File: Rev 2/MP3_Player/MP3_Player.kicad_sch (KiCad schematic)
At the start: 1 part, among them U1 ESP32-WROOM-32

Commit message: added some parts
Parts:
- added J1: AudioJack3_SwitchT, symbol Connector_Audio:AudioJack3_SwitchT
- added M1: Haptic Feedback, symbol Motor:Motor_DC
- added SW1: RotaryEncoder_Switch, symbol Device:RotaryEncoder_Switch
- added SW2, SW3, SW4, SW5: SW_SPST, symbol Switch:SW_SPST
- added U2: ~, Subsystem Main:2.4'_TFT_SPI_ILI9341_WITH_SD_CARD, symbol MP3_Player_Custom_Parts:2.4'_TFT_SPI_ILI9341_WITH_SD_CARD

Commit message: Finished Setup
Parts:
- added L_SPKR1, RSPKR1: ~, MP3_Player_Custom_Footprints:MAX98357 I2C Audio Driver, symbol MP3_Player_Custom_Parts:Adafruit_MAX98357
- added Q1: NPN, Package_TO_SOT_THT:TO-92L_Inline, symbol Simulation_SPICE:NPN
- added R1, R2, R3, R4, R5, R6: 10K, Resistor_THT:R_Axial_DIN0204_L3.6mm_D1.6mm_P7.62mm_Horizontal, symbol Device:R
- added R7: R, Resistor_THT:R_Axial_DIN0204_L3.6mm_D1.6mm_P7.62mm_Horizontal, symbol Device:R
- added SW4: Power, Button_Switch_THT:SW_Slide_SPDT_Angled_CK_OS102011MA1Q, symbol Switch:SW_SPDT
- added SW6: Hold, Button_Switch_THT:SW_Slide_SPDT_Angled_CK_OS102011MA1Q, symbol Switch:SW_SPDT
- ESP32: renamed from U1; footprint RF_Module:ESP32-WROOM-32 -> MP3_Player_Custom_Footprints:Wemos Lolin32 Lite v1.0.0
- J1: footprint (none) -> Connector_Audio:Jack_3.5mm_CUI_SJ1-3524N_Horizontal
- M1: footprint (none) -> TerminalBlock_RND:TerminalBlock_RND_205-00001_1x02_P5.00mm_Horizontal
- Primary Rotary Encoder1: renamed from SW1; footprint (none) -> Rotary_Encoder:RotaryEncoder_Alps_EC11E-Switch_Vertical_H20mm
- SW1: renamed from SW2; value SW_SPST -> Home; footprint (none) -> keyswitches:Kailh_socket_PG1350
- SW2: renamed from SW4; value SW_SPST -> Back; footprint (none) -> keyswitches:Kailh_socket_PG1350
- SW3: value SW_SPST -> Play/Pause; footprint (none) -> keyswitches:Kailh_socket_PG1350
- SW5: value SW_SPST -> Menu; footprint (none) -> keyswitches:Kailh_socket_PG1350
- Screen&SDCardReader1: renamed from U2; footprint Subsystem Main:2.4'_TFT_SPI_ILI9341_WITH_SD_CARD -> MP3_Player_Custom_Footprints:2.4'_TFT_SPI_ILI9341_WITH_SD_CARD
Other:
- moved on the sheet: ESP32, J1, M1, Primary Rotary Encoder1, SW1, SW2, SW3, SW5, Screen&SDCardReader1

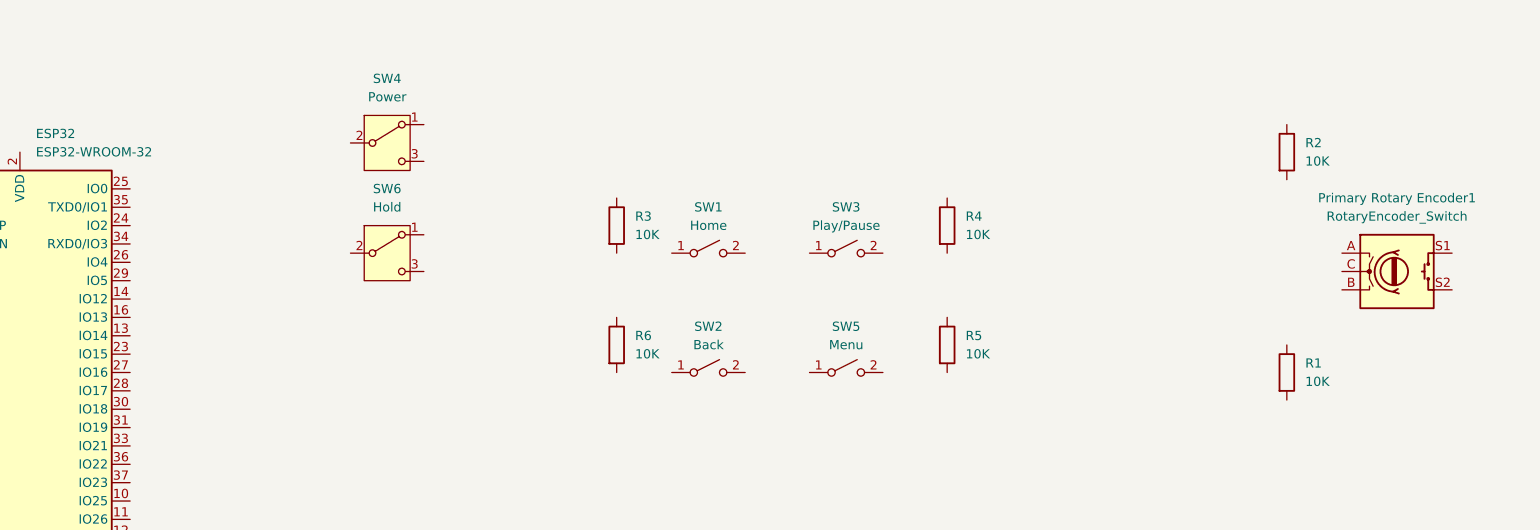
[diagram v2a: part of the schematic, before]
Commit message: W/ Wired Rotary Encoder
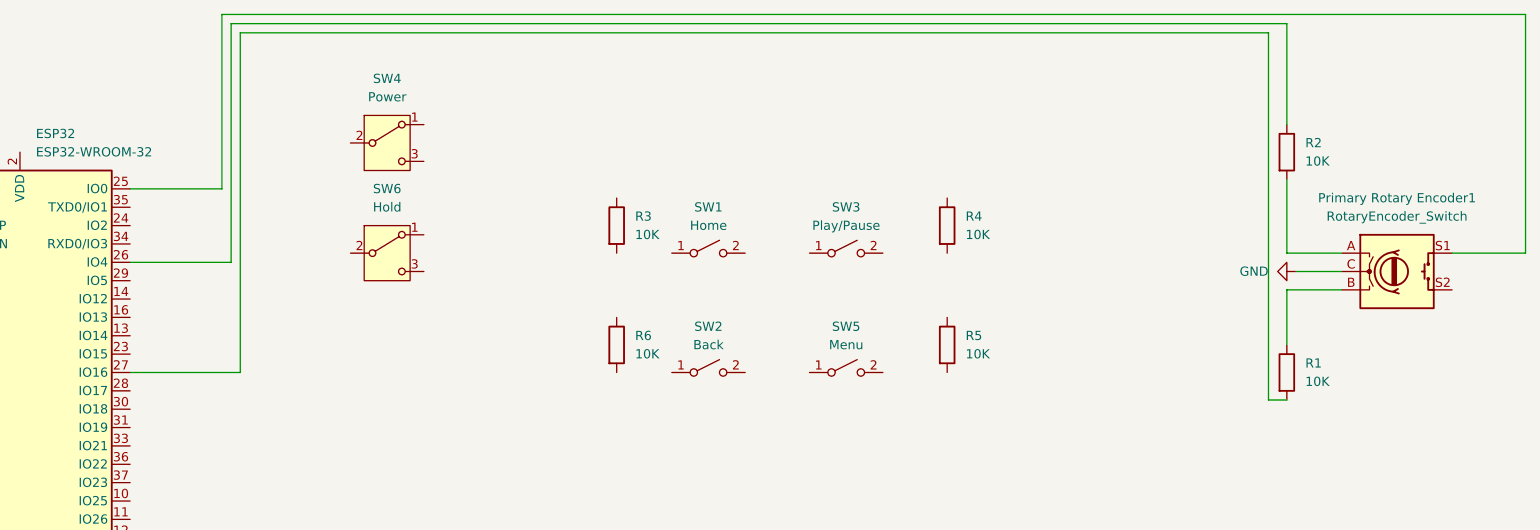
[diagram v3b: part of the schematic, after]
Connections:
- net at R2.1: now also ESP32.26 (IO4)
- net at R2.2: now also Primary Rotary Encoder1.A
- net at Primary Rotary Encoder1.B: now also R1.1
- net GND: now reaches Primary Rotary Encoder1.C
- net at Primary Rotary Encoder1.S1: now also ESP32.25 (IO0)
- net at R1.2: now also ESP32.27 (IO16)
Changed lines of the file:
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@@
 	(generator_version "8.0")
 	(paper "A4")
+	(wire
+		(pts
+			(xy 242.57 27.94) (xy 242.57 13.97)
+		)
+		(stroke
+			(width 0)
+			(type default)
+		)
+	)
+	(wire
+		(pts
+			(xy 95.25 36.83) (xy 95.25 12.7)
+		)
+		(stroke
+			(width 0)
+			(type default)
+		)
+	)
+	(wire
+		(pts
+			(xy 275.59 12.7) (xy 275.59 45.72)
+		)
+		(stroke
+			(width 0)
+			(type default)
+		)
+	)
+	(wire
+		(pts
+			(xy 95.25 12.7) (xy 275.59 12.7)
+		)
+		(stroke
+			(width 0)
+			(type default)
+		)
+	)
+	(wire
+		(pts
+			(xy 82.55 46.99) (xy 96.52 46.99)
+		)
+		(stroke
+			(width 0)
+			(type default)
+		)
+	)
+	(wire
+		(pts
+			(xy 250.19 50.8) (xy 242.57 50.8)
+		)
+		(stroke
+			(width 0)
+			(type default)
+		)
+	)
+	(wire
+		(pts
+			(xy 82.55 62.23) (xy 97.79 62.23)
+		)
+		(stroke
+			(width 0)
+			(type default)
+		)
+	)
+	(wire
+		(pts
+			(xy 240.03 15.24) (xy 240.03 66.04)
+		)
+		(stroke
+			(width 0)
+			(type default)
+		)
+	)
+	(wire
+		(pts
+			(xy 97.79 15.24) (xy 240.03 15.24)
+		)
+		(stroke
+			(width 0)
+			(type default)
+		)
+	)
+	(wire
+		(pts
+			(xy 242.57 13.97) (xy 96.52 13.97)
+		)
+		(stroke
+			(width 0)
+			(type default)
+		)
+	)
+	(wire
+		(pts
+			(xy 275.59 45.72) (xy 265.43 45.72)
+		)
+		(stroke
+			(width 0)
+			(type default)
+		)
+	)
+	(wire
+		(pts
+			(xy 250.19 45.72) (xy 242.57 45.72)
+		)
+		(stroke
+			(width 0)
+			(type default)
+		)
+	)
+	(wire
+		(pts
+			(xy 243.84 48.26) (xy 250.19 48.26)
+		)
+		(stroke
+			(width 0)
+			(type default)
+		)
+	)
+	(wire
+		(pts
+			(xy 96.52 13.97) (xy 96.52 46.99)
+		)
+		(stroke
+			(width 0)
+			(type default)
+		)
+	)
+	(wire
+		(pts
+			(xy 97.79 62.23) (xy 97.79 15.24)
+		)
+		(stroke
+			(width 0)
+			(type default)
+		)
+	)
+	(wire
+		(pts
+			(xy 82.55 36.83) (xy 95.25 36.83)
+		)
+		(stroke
+			(width 0)
+			(type default)
+		)
+	)
+	(wire
+		(pts
+			(xy 242.57 45.72) (xy 242.57 35.56)
+		)
+		(stroke
+			(width 0)
+			(type default)
+		)
+	)
+	(wire
+		(pts
+			(xy 242.57 50.8) (xy 242.57 58.42)
+		)
+		(stroke
+			(width 0)
+			(type default)
+		)
+	)
+	(wire
+		(pts
+			(xy 240.03 66.04) (xy 242.57 66.04)
+		)
+		(stroke
+			(width 0)
+			(type default)
+		)
+	)
 	(symbol
 		(lib_id "Device:R")
@@
 					(unit 1)
 				)
+			)
+		)
+	)
+	(symbol
+		(lib_id "power:GND")
+		(at 243.84 48.26 270)
+		(unit 1)
+		(exclude_from_sim no)
+		(in_bom yes)
+		(on_board yes)
+		(dnp no)
+		(fields_autoplaced yes)
+		(property "Reference" "#PWR01"
+			(at 237.49 48.26 0)
+			(effects
+				(font
+					(size 1.27 1.27)
+				)
+				(hide yes)
+			)
+		)
+		(property "Value" "GND"
+			(at 240.03 48.2599 90)
+			(effects
+				(font
+					(size 1.27 1.27)
+				)
+				(justify right)
+			)
+		)
+		(property "Footprint" ""
+			(at 243.84 48.26 0)
+			(effects
+				(font
+					(size 1.27 1.27)
+				)
+				(hide yes)
+			)
+		)
+		(property "Datasheet" ""
+			(at 243.84 48.26 0)
+			(effects
+				(font
+					(size 1.27 1.27)
+				)
+				(hide yes)
+			)
+		)
+		(property "Description" "Power symbol creates a global label with name \"GND\" , ground"
+			(at 243.84 48.26 0)
+			(effects
+				(font
+					(size 1.27 1.27)
+				)
+				(hide yes)
+			)
+		)
+		(pin "1"
+		)
+		(instances
+			(project ""
+				(path "/caa12bce-cf4c-4041-a9a3-d1ebb8f4f00b"
+					(reference "#PWR01")
+					(unit 1)
+				)

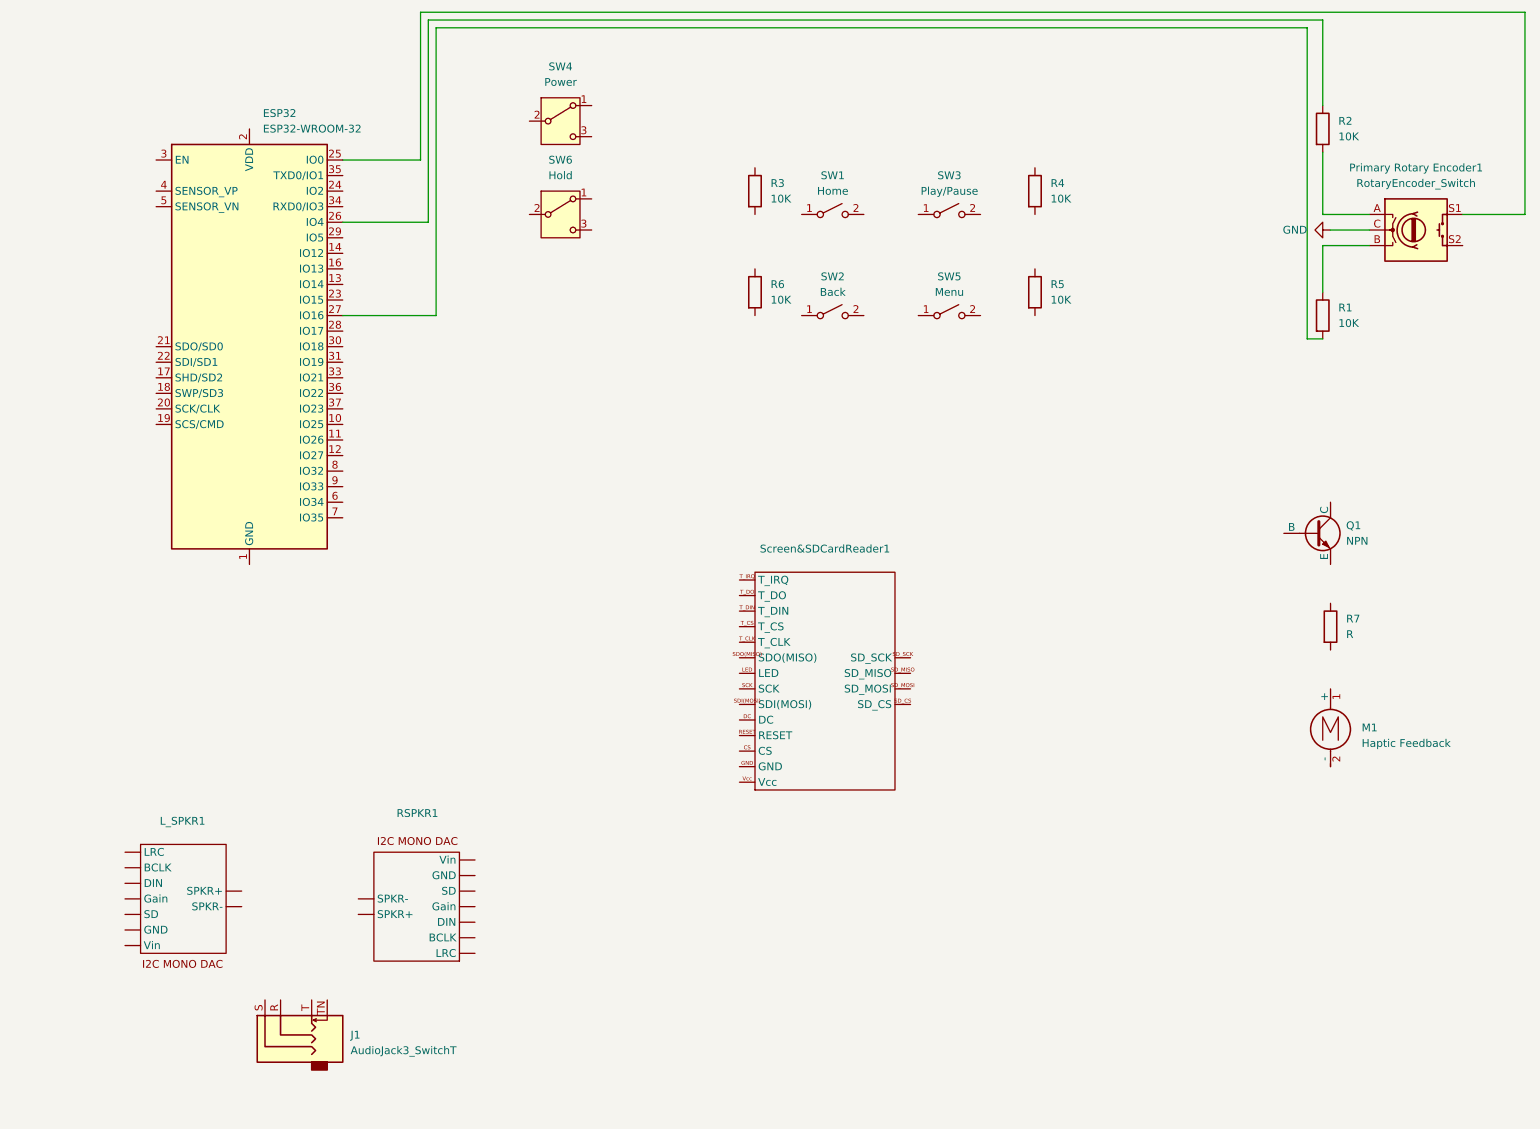
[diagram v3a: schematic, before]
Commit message: W/ Wired Rotary Encoder Switches & Keys
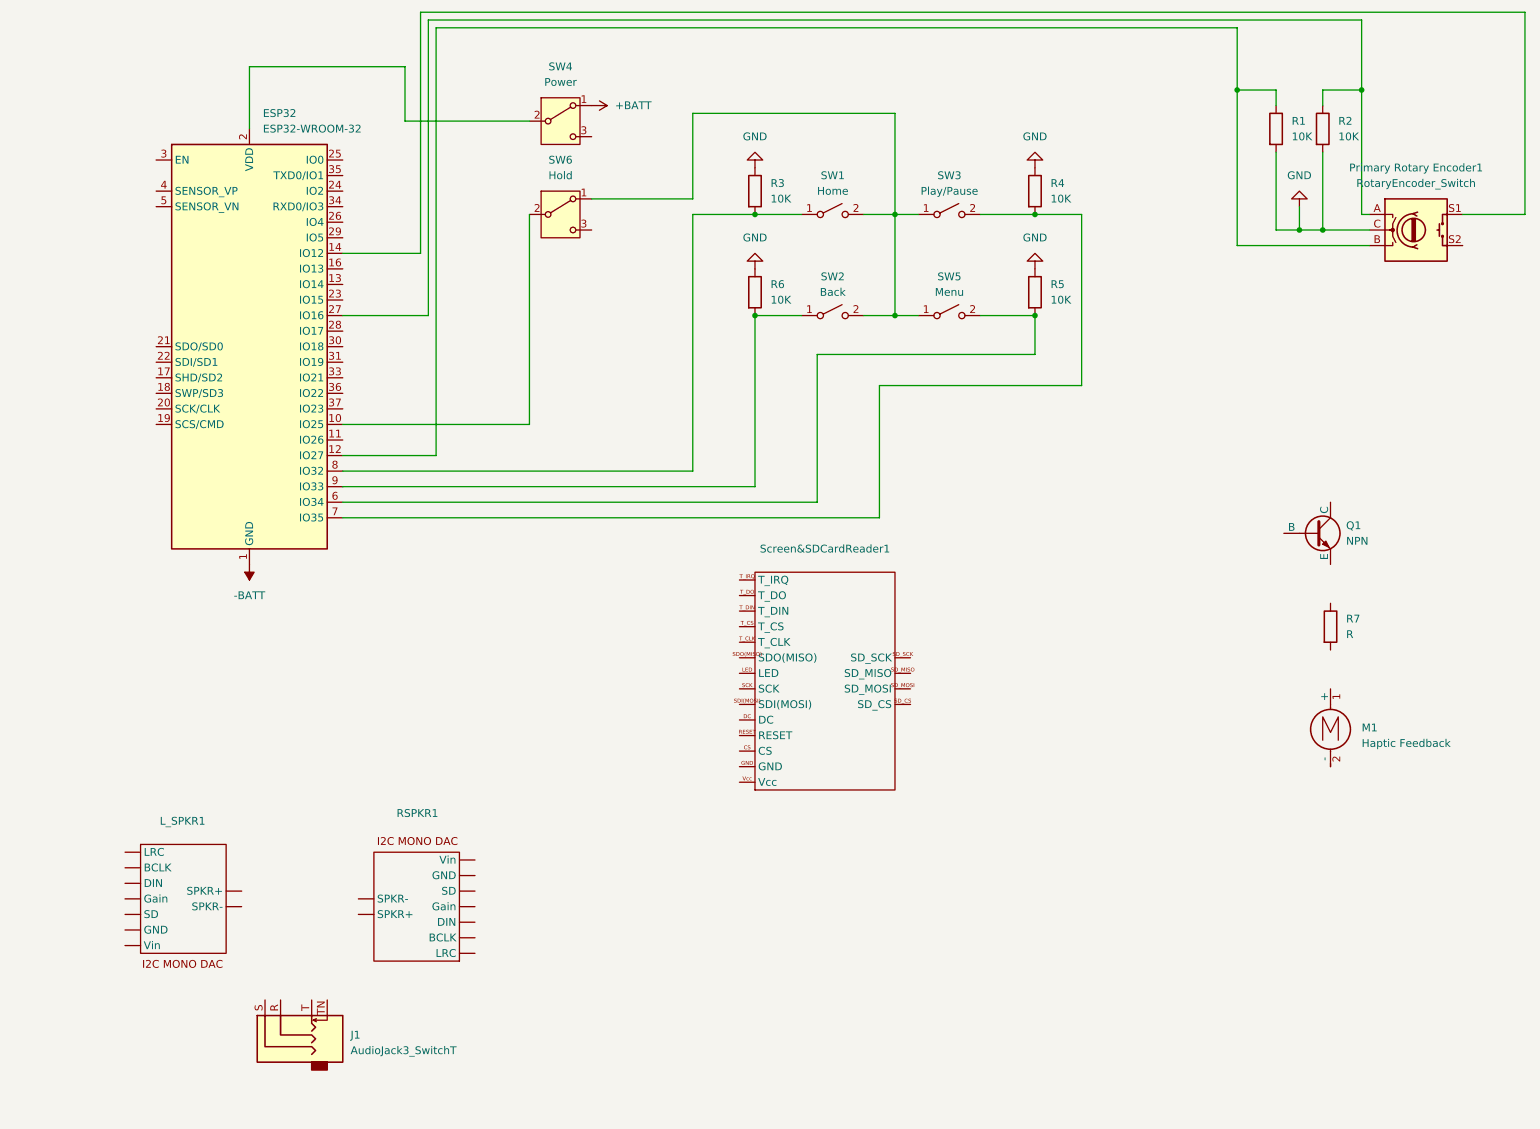
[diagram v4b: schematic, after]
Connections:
- net GND: now also R1.2, R2.2, R3.1, R4.1, R5.1, R6.1
- net at R2.1: now also ESP32.27 (IO16), Primary Rotary Encoder1.A; no longer ESP32.26 (IO4)
- net at R4.2: now also ESP32.7 (IO35), SW3.2 (B)
- net at SW1.1 (A): now also ESP32.8 (IO32), R3.2
- net at SW1.2 (B): now also SW2.2 (B), SW3.1 (A), SW5.1 (A), SW6.1 (A)
- net at SW2.1 (A): now also ESP32.9 (IO33), R6.2
- net at Primary Rotary Encoder1.B, R1.1: now also ESP32.12 (IO27)
- net at Primary Rotary Encoder1.S1: now also ESP32.14 (IO12); no longer ESP32.25 (IO0)
- net at SW6.2 (B): now also ESP32.10 (IO25)
- net at SW5.2 (B): now also ESP32.6 (IO34), R5.2
- net -BATT: now reaches ESP32.1 (GND), ESP32.15 (GND), ESP32.38 (GND), ESP32.39 (GND)
- net at ESP32.2 (VDD): now also SW4.2 (B)
- net +BATT: now reaches SW4.1 (A)
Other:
- moved on the sheet: R1

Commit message: Added pullup on the buttons
And also a pulldown resistor on the rotary encoder
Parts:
- added R8: 10K, Resistor_THT:R_Axial_DIN0204_L3.6mm_D1.6mm_P7.62mm_Horizontal, symbol Device:R
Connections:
- net GND: now also R8.1
- net VDD: now reaches SW1.2 (B), SW2.2 (B), SW3.1 (A), SW5.1 (A), SW6.1 (A)
- net VDD: now also ESP32.2 (VDD), Primary Rotary Encoder1.S2, SW4.2 (B)
- net at ESP32.14 (IO12), Primary Rotary Encoder1.S1: now also R8.2
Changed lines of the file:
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@@
+	)
+	(junction
+		(at 275.59 30.48)
+		(diameter 0)
+		(color 0 0 0 0)
 	)
 	(junction
@@
 	(wire
 		(pts
-			(xy 275.59 12.7) (xy 275.59 45.72)
+			(xy 275.59 12.7) (xy 275.59 30.48)
 		)
 		(stroke
@@
 	(wire
 		(pts
+			(xy 275.59 30.48) (xy 275.59 45.72)
+		)
+		(stroke
+			(width 0)
+			(type default)
+			(color 57 191 251 1)
+		)
+	)
+	(wire
+		(pts
 			(xy 97.79 15.24) (xy 228.6 15.24)
 		)
@@
 			(type default)
 			(color 233 72 52 1)
+		)
+	)
+	(label "VDD"
+		(at 67.31 31.75 90)
+		(fields_autoplaced yes)
+		(effects
+			(font
+				(size 1.27 1.27)
+			)
+			(justify left bottom)
+		)
+	)
+	(label "VDD"
+		(at 265.43 50.8 0)
+		(fields_autoplaced yes)
+		(effects
+			(font
+				(size 1.27 1.27)
+			)
+			(justify left bottom)
+		)
+	)
+	(label "VDD"
+		(at 172.72 45.72 180)
+		(fields_autoplaced yes)
+		(effects
+			(font
+				(size 1.27 1.27)
+			)
+			(justify right bottom)
 		)
 	)
@@
 	(symbol
 		(lib_id "Device:R")
+		(at 271.78 30.48 90)
+		(unit 1)
+		(exclude_from_sim no)
+		(in_bom yes)
+		(on_board yes)
+		(dnp no)
+		(fields_autoplaced yes)
+		(property "Reference" "R8"
+			(at 270.5099 27.94 0)
+			(effects
+				(font
+					(size 1.27 1.27)
+				)
+				(justify left)
+			)
+		)
+		(property "Value" "10K"
+			(at 273.0499 27.94 0)
+			(effects
+				(font
+					(size 1.27 1.27)
+				)
+				(justify left)
+			)
+		)
+		(property "Footprint" "Resistor_THT:R_Axial_DIN0204_L3.6mm_D1.6mm_P7.62mm_Horizontal"
+			(at 271.78 32.258 90)
+			(effects
+				(font
+					(size 1.27 1.27)
+				)
+				(hide yes)
+			)
+		)
+		(property "Datasheet" "~"
+			(at 271.78 30.48 0)
+			(effects
+				(font
+					(size 1.27 1.27)
+				)
+				(hide yes)
+			)
+		)
+		(property "Description" "Resistor"
+			(at 271.78 30.48 0)
+			(effects
+				(font
+					(size 1.27 1.27)
+				)
+				(hide yes)
+			)
+		)
+		(pin "1"
+		)
+		(pin "2"
+		)
+		(instances
+			(project "MP3_Player"
+				(path "/caa12bce-cf4c-4041-a9a3-d1ebb8f4f00b"
+					(reference "R8")
+					(unit 1)
+				)
+			)
+		)
+	)
+	(symbol
+		(lib_id "Device:R")
 		(at 195.58 41.91 0)
 		(unit 1)
@@
 					(unit 1)
 				)
+			)
+		)
+	)
+	(symbol
+		(lib_id "power:GND")
+		(at 267.97 30.48 270)
+		(unit 1)
+		(exclude_from_sim no)
+		(in_bom yes)
+		(on_board yes)
+		(dnp no)
+		(fields_autoplaced yes)
+		(property "Reference" "#PWR08"
+			(at 261.62 30.48 0)
+			(effects
+				(font
+					(size 1.27 1.27)
+				)
+				(hide yes)
+			)
+		)
+		(property "Value" "GND"
+			(at 262.89 30.48 0)
+			(effects
+				(font
+					(size 1.27 1.27)
+				)
+			)
+		)
+		(property "Footprint" ""
+			(at 267.97 30.48 0)
+			(effects
+				(font
+					(size 1.27 1.27)
+				)
+				(hide yes)
+			)
+		)
+		(property "Datasheet" ""
+			(at 267.97 30.48 0)
+			(effects
+				(font
+					(size 1.27 1.27)
+				)
+				(hide yes)
+			)
+		)
+		(property "Description" "Power symbol creates a global label with name \"GND\" , ground"
+			(at 267.97 30.48 0)
+			(effects
+				(font
+					(size 1.27 1.27)
+				)
+				(hide yes)
+			)
+		)
+		(pin "1"
+		)
+		(instances
+			(project "MP3_Player"
+				(path "/caa12bce-cf4c-4041-a9a3-d1ebb8f4f00b"
+					(reference "#PWR08")
+					(unit 1)
+				)
